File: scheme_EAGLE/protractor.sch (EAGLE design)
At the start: 2 parts

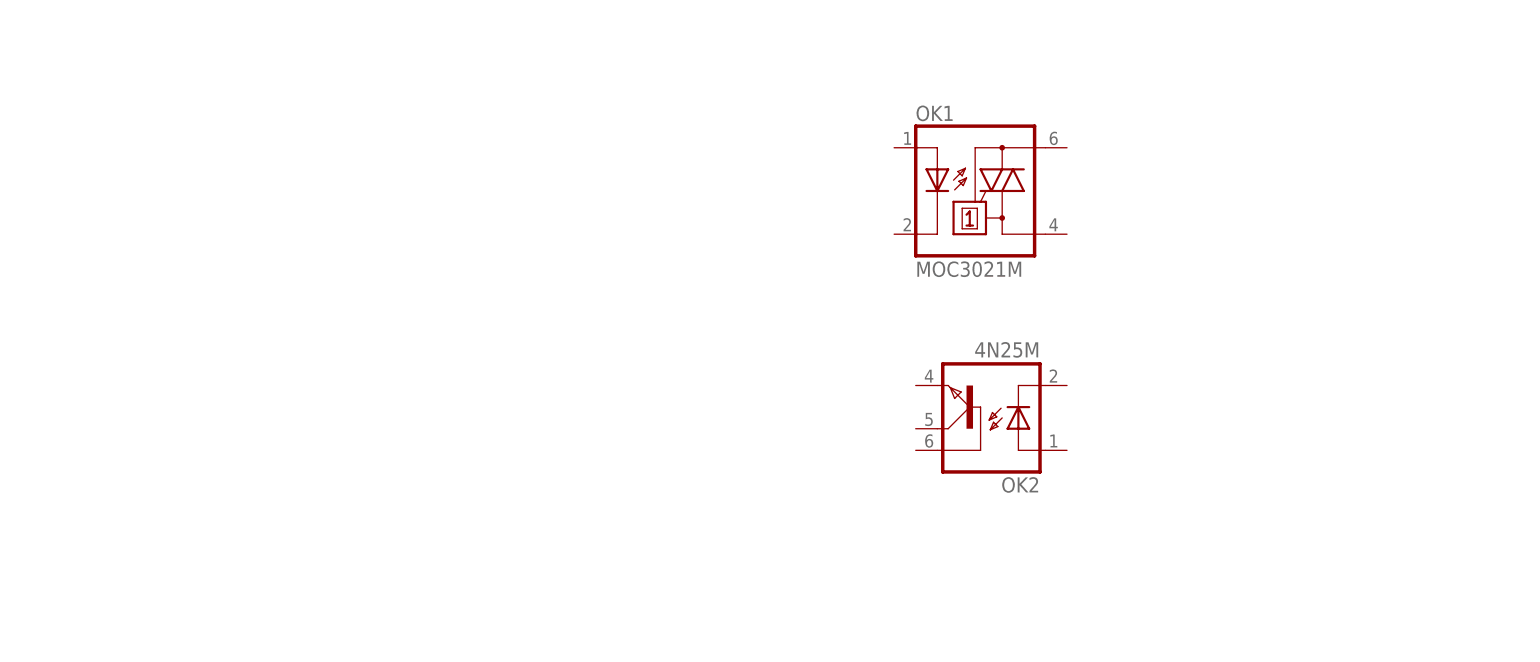
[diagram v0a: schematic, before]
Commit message: Added the bridge retifier and BT137.
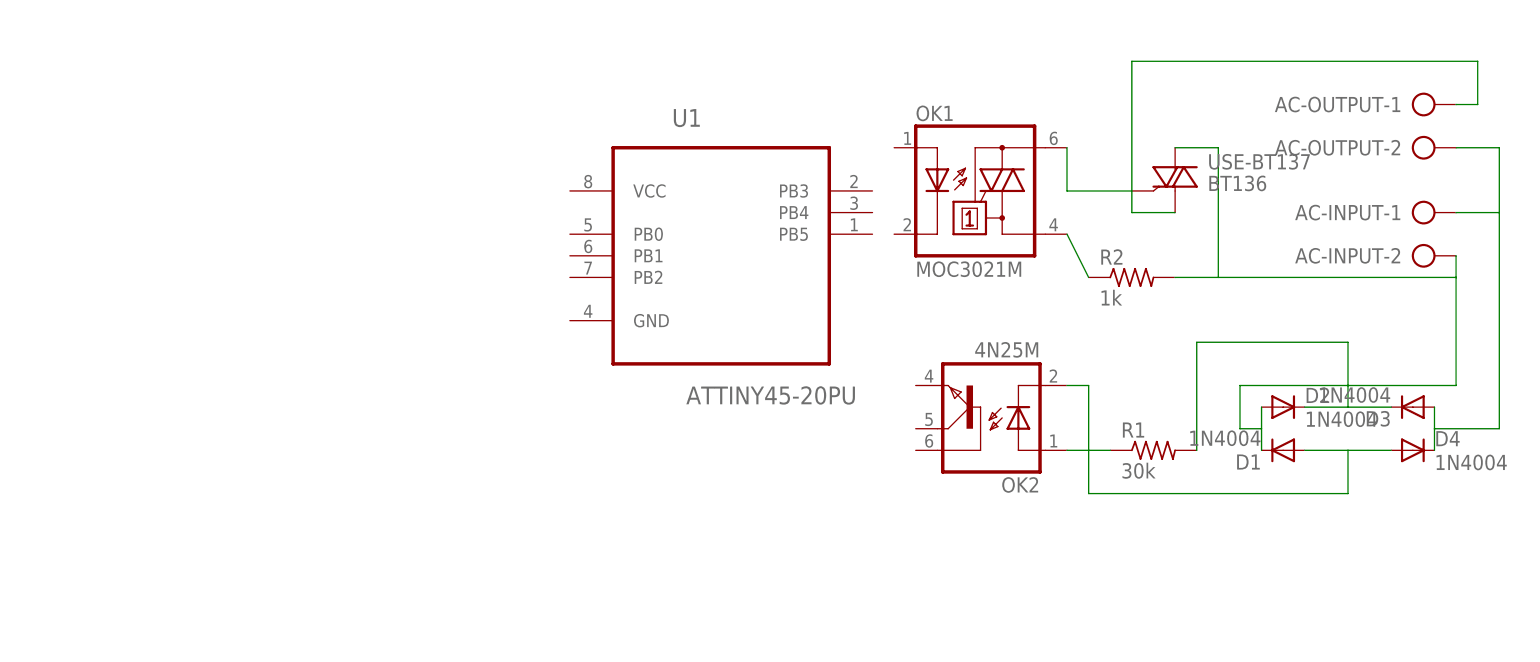
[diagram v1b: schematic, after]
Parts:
- added AC-INPUT, AC-OUTPUT: (no value), con-ptr500:AK500/2-H
- added D1, D2, D3, D4: 1N4004, adafruit:1N4004
- added R1: 30k, adafruit:R-US_0207/12
- added R2: 1k, adafruit:R-US_0207/12
- added U1: ATTINY45-20PU, Atmel_By_element14_Batch_1-00:ATTINY45-20PU
- added USE-BT137: BT136, triac:BT136
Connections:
- new net N$1: D1.A, D4.A, OK2.C
- new net N$2: D2.C, D3.C, R1.2
- new net N$3: AC-INPUT-1.KL, AC-OUTPUT-2.KL, D3.A, D4.C
- new net N$4: AC-INPUT-2.KL, D1.C, D2.A, R2.2, USE-BT137.A2
- new net N$5: OK2.A, R1.1
- new net N$6: OK1.A2, USE-BT137.G
- new net N$7: OK1.A1, R2.1
- new net N$8: AC-OUTPUT-1.KL, USE-BT137.A1

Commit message: Schema done, inserted news components.
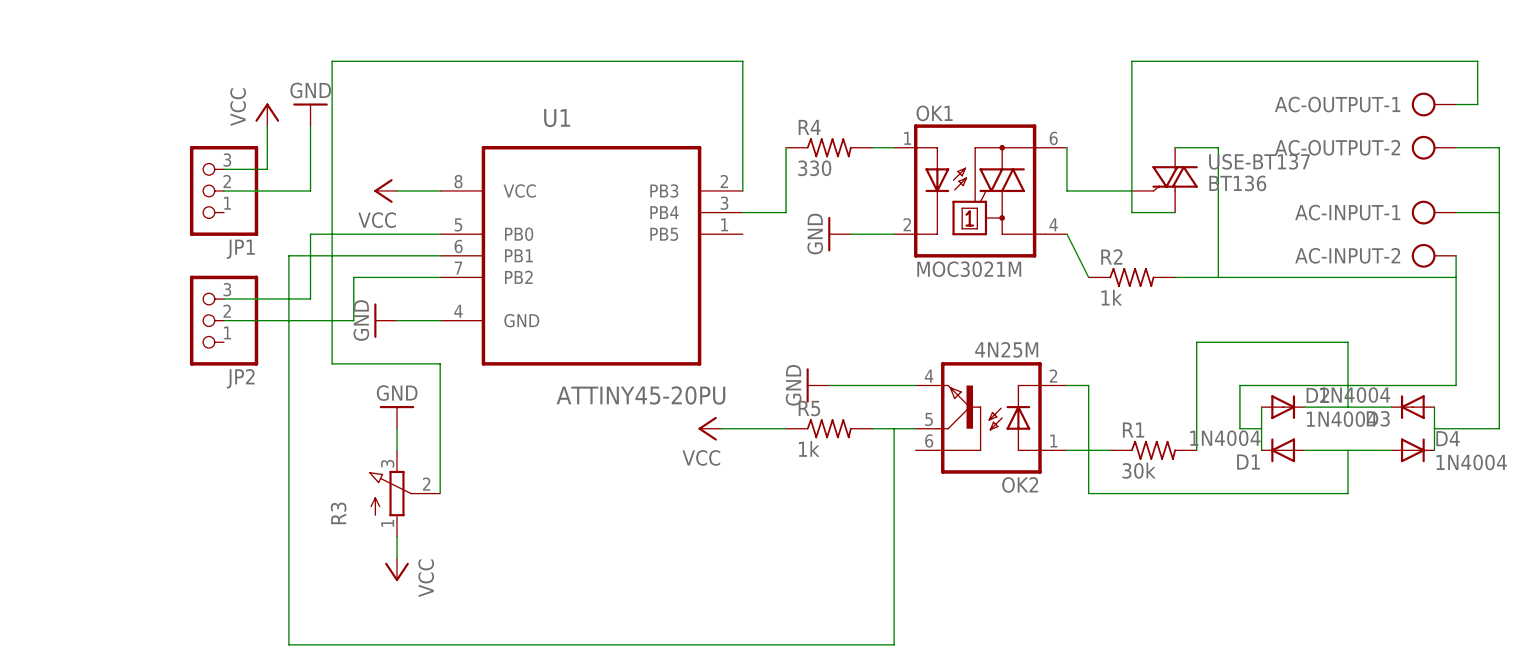
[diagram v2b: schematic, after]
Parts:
- added JP1, JP2: (no value), adafruit:PINHD-1X3
- added R3: (no value), pot:3RP/1610N
- added R4: 330, adafruit:R-US_0207/12
- added R5: 1k, adafruit:R-US_0207/12
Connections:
- new net GND: JP1.2, OK1.C, OK2.EMI, R3.E, U1.GND
- new net N$10: OK2.COL, R5.2, U1.PB1
- new net N$11: JP2.2, U1.PB2
- new net N$12: R4.1, U1.PB4
- new net N$13: OK1.A, R4.2
- new net N$14: JP2.3, U1.PB0
- new net N$9: R3.S, U1.PB3
- new net VCC: JP1.3, R3.A, R5.1, U1.VCC
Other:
- moved on the sheet: U1
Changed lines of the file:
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@@
 <part name="R2" library="adafruit" deviceset="R-US_" device="0207/12" value="1k"/>
 <part name="U1" library="Atmel_By_element14_Batch_1-00" deviceset="ATTINY45-20PU" device=""/>
+<part name="R3" library="pot" deviceset="3RP/1610N" device=""/>
+<part name="JP1" library="adafruit" deviceset="PINHD-1X3" device=""/>
+<part name="P+1" library="supply1" deviceset="VCC" device=""/>
+<part name="GND1" library="supply1" deviceset="GND" device=""/>
+<part name="GND2" library="supply1" deviceset="GND" device=""/>
+<part name="P+2" library="supply1" deviceset="VCC" device=""/>
+<part name="GND3" library="supply1" deviceset="GND" device=""/>
+<part name="P+3" library="supply1" deviceset="VCC" device=""/>
+<part name="R4" library="adafruit" deviceset="R-US_" device="0207/12" value="330"/>
+<part name="P+4" library="supply1" deviceset="VCC" device=""/>
+<part name="R5" library="adafruit" deviceset="R-US_" device="0207/12" value="1k"/>
+<part name="GND4" library="supply1" deviceset="GND" device=""/>
+<part name="GND5" library="supply1" deviceset="GND" device=""/>
+<part name="JP2" library="adafruit" deviceset="PINHD-1X3" device=""/>
 </parts>
 <sheets>
@@
 <instance part="AC-INPUT" gate="-2" x="104.14" y="68.58"/>
 <instance part="R2" gate="G$1" x="71.12" y="66.04"/>
-<instance part="U1" gate="A" x="22.86" y="71.12"/>
+<instance part="U1" gate="A" x="7.62" y="71.12"/>
+<instance part="R3" gate="G$1" x="-15.24" y="40.64"/>
+<instance part="JP1" gate="A" x="-38.1" y="76.2" rot="R180"/>
+<instance part="P+1" gate="VCC" x="-30.48" y="86.36"/>
+<instance part="GND1" gate="1" x="-25.4" y="86.36" rot="R180"/>
+<instance part="GND2" gate="1" x="-15.24" y="50.8" rot="R180"/>
+<instance part="P+2" gate="VCC" x="-15.24" y="30.48" rot="R180"/>
+<instance part="GND3" gate="1" x="-17.78" y="60.96" rot="R270"/>
+<instance part="P+3" gate="VCC" x="-17.78" y="76.2" rot="R90"/>
+<instance part="R4" gate="G$1" x="35.56" y="81.28"/>
+<instance part="P+4" gate="VCC" x="20.32" y="48.26" rot="R90"/>
+<instance part="R5" gate="G$1" x="35.56" y="48.26"/>
+<instance part="GND4" gate="1" x="33.02" y="53.34" rot="R270"/>
+<instance part="GND5" gate="1" x="35.56" y="71.12" rot="R270"/>
+<instance part="JP2" gate="A" x="-38.1" y="60.96" rot="R180"/>
 </instances>
 <busses>
@@
 </segment>
 </net>
+<net name="N$9" class="0">
+<segment>
+<pinref part="R3" gate="G$1" pin="S"/>
+<wire x1="-10.16" y1="40.64" x2="-10.16" y2="55.88" width="0.1524" layer="91"/>
+<wire x1="-10.16" y1="55.88" x2="-22.86" y2="55.88" width="0.1524" layer="91"/>
+<wire x1="-22.86" y1="55.88" x2="-22.86" y2="91.44" width="0.1524" layer="91"/>
+<pinref part="U1" gate="A" pin="PB3"/>
+<wire x1="-22.86" y1="91.44" x2="25.4" y2="91.44" width="0.1524" layer="91"/>
+<wire x1="25.4" y1="91.44" x2="25.4" y2="76.2" width="0.1524" layer="91"/>
+</segment>
+</net>
+<net name="GND" class="0">
+<segment>
+<pinref part="R3" gate="G$1" pin="E"/>
+<pinref part="GND2" gate="1" pin="GND"/>
+<wire x1="-15.24" y1="48.26" x2="-15.24" y2="45.72" width="0.1524" layer="91"/>
+</segment>
+<segment>
+<pinref part="JP1" gate="A" pin="2"/>
+<pinref part="GND1" gate="1" pin="GND"/>
+<wire x1="-35.56" y1="76.2" x2="-25.4" y2="76.2" width="0.1524" layer="91"/>
+<wire x1="-25.4" y1="76.2" x2="-25.4" y2="83.82" width="0.1524" layer="91"/>
+</segment>
+<segment>
+<pinref part="U1" gate="A" pin="GND"/>
+<pinref part="GND3" gate="1" pin="GND"/>
+<wire x1="-10.16" y1="60.96" x2="-15.24" y2="60.96" width="0.1524" layer="91"/>
+</segment>
+<segment>
+<pinref part="OK2" gate="G$1" pin="EMI"/>
+<pinref part="GND4" gate="1" pin="GND"/>
+<wire x1="45.72" y1="53.34" x2="35.56" y2="53.34" width="0.1524" layer="91"/>
+</segment>
+<segment>
+<pinref part="OK1" gate="-1" pin="C"/>
+<pinref part="GND5" gate="1" pin="GND"/>
+<wire x1="43.18" y1="71.12" x2="38.1" y2="71.12" width="0.1524" layer="91"/>
+</segment>
+</net>
+<net name="VCC" class="0">
+<segment>
+<pinref part="R3" gate="G$1" pin="A"/>
+<pinref part="P+2" gate="VCC" pin="VCC"/>
+<wire x1="-15.24" y1="35.56" x2="-15.24" y2="33.02" width="0.1524" layer="91"/>
+</segment>
+<segment>
+<pinref part="JP1" gate="A" pin="3"/>
+<pinref part="P+1" gate="VCC" pin="VCC"/>
+<wire x1="-35.56" y1="78.74" x2="-30.48" y2="78.74" width="0.1524" layer="91"/>
+<wire x1="-30.48" y1="78.74" x2="-30.48" y2="83.82" width="0.1524" layer="91"/>
+</segment>
+<segment>
+<pinref part="U1" gate="A" pin="VCC"/>
+<pinref part="P+3" gate="VCC" pin="VCC"/>
+<wire x1="-10.16" y1="76.2" x2="-15.24" y2="76.2" width="0.1524" layer="91"/>
+</segment>
+<segment>
+<pinref part="R5" gate="G$1" pin="1"/>
+<pinref part="P+4" gate="VCC" pin="VCC"/>
+<wire x1="30.48" y1="48.26" x2="22.86" y2="48.26" width="0.1524" layer="91"/>
+</segment>
+</net>
+<net name="N$10" class="0">
+<segment>
+<pinref part="R5" gate="G$1" pin="2"/>
+<pinref part="OK2" gate="G$1" pin="COL"/>
+<wire x1="40.64" y1="48.26" x2="43.18" y2="48.26" width="0.1524" layer="91"/>
+<pinref part="U1" gate="A" pin="PB1"/>
+<wire x1="43.18" y1="48.26" x2="45.72" y2="48.26" width="0.1524" layer="91"/>
+<wire x1="-10.16" y1="68.58" x2="-27.94" y2="68.58" width="0.1524" layer="91"/>
+<wire x1="-27.94" y1="68.58" x2="-27.94" y2="22.86" width="0.1524" layer="91"/>
+<wire x1="-27.94" y1="22.86" x2="43.18" y2="22.86" width="0.1524" layer="91"/>
+<wire x1="43.18" y1="22.86" x2="43.18" y2="48.26" width="0.1524" layer="91"/>
+</segment>
+</net>
+<net name="N$12" class="0">
+<segment>
+<pinref part="U1" gate="A" pin="PB4"/>
+<pinref part="R4" gate="G$1" pin="1"/>
+<wire x1="25.4" y1="73.66" x2="30.48" y2="73.66" width="0.1524" layer="91"/>
+<wire x1="30.48" y1="73.66" x2="30.48" y2="81.28" width="0.1524" layer="91"/>
+</segment>
+</net>
+<net name="N$13" class="0">
+<segment>
+<pinref part="R4" gate="G$1" pin="2"/>
+<pinref part="OK1" gate="-1" pin="A"/>
+<wire x1="40.64" y1="81.28" x2="43.18" y2="81.28" width="0.1524" layer="91"/>
+</segment>
+</net>
+<net name="N$14" class="0">
+<segment>
+<pinref part="JP2" gate="A" pin="3"/>
+<wire x1="-35.56" y1="63.5" x2="-25.4" y2="63.5" width="0.1524" layer="91"/>
+<wire x1="-25.4" y1="63.5" x2="-25.4" y2="71.12" width="0.1524" layer="91"/>
+<pinref part="U1" gate="A" pin="PB0"/>
+<wire x1="-25.4" y1="71.12" x2="-10.16" y2="71.12" width="0.1524" layer="91"/>
+</segment>
+</net>
+<net name="N$11" class="0">
+<segment>
+<pinref part="JP2" gate="A" pin="2"/>
+<wire x1="-35.56" y1="60.96" x2="-20.32" y2="60.96" width="0.1524" layer="91"/>
+<wire x1="-20.32" y1="60.96" x2="-20.32" y2="66.04" width="0.1524" layer="91"/>
+<pinref part="U1" gate="A" pin="PB2"/>
+<wire x1="-20.32" y1="66.04" x2="-10.16" y2="66.04" width="0.1524" layer="91"/>
+</segment>
+</net>

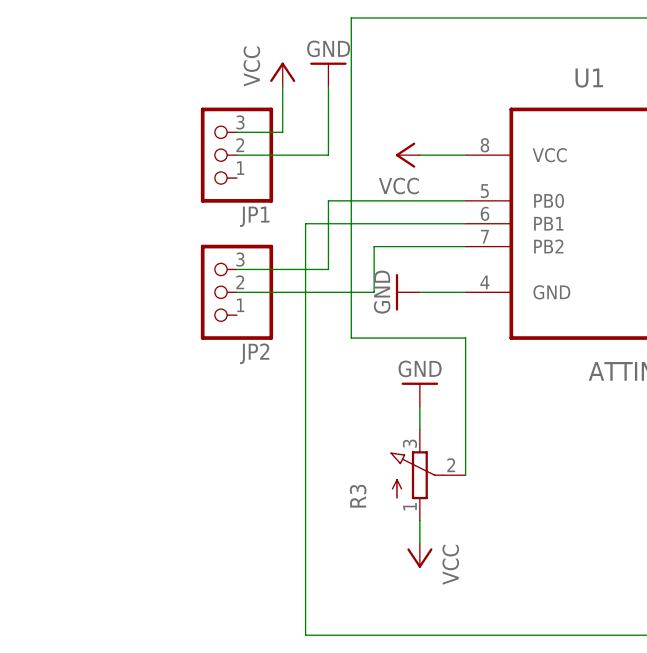
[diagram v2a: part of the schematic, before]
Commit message: Inserted the switch to choose between Arduino Comands and Potentiometer
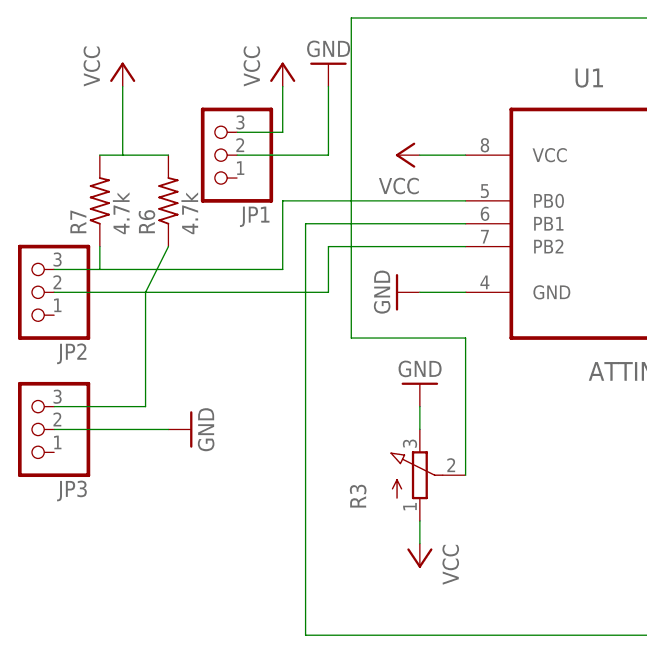
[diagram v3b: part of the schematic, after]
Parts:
- added JP3: (no value), adafruit:PINHD-1X3
- added R6, R7: 4.7k, adafruit:R-US_0207/12
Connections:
- net GND: now also JP3.2
- net N$11: now also JP2.3, R7.1, U1.PB0; no longer JP2.2, U1.PB2
- net N$14: now also JP2.2, JP3.3, R6.1, U1.PB2; no longer JP2.3, U1.PB0
- net VCC: now also R6.2, R7.2
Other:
- moved on the sheet: JP2
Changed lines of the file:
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@@
 <part name="GND5" library="supply1" deviceset="GND" device=""/>
 <part name="JP2" library="adafruit" deviceset="PINHD-1X3" device=""/>
+<part name="JP3" library="adafruit" deviceset="PINHD-1X3" device=""/>
+<part name="R6" library="adafruit" deviceset="R-US_" device="0207/12" value="4.7k"/>
+<part name="R7" library="adafruit" deviceset="R-US_" device="0207/12" value="4.7k"/>
+<part name="P+5" library="supply1" deviceset="VCC" device=""/>
+<part name="GND6" library="supply1" deviceset="GND" device=""/>
 </parts>
 <sheets>
@@
 <instance part="GND4" gate="1" x="33.02" y="53.34" rot="R270"/>
 <instance part="GND5" gate="1" x="35.56" y="71.12" rot="R270"/>
-<instance part="JP2" gate="A" x="-38.1" y="60.96" rot="R180"/>
+<instance part="JP2" gate="A" x="-58.42" y="60.96" rot="R180"/>
+<instance part="JP3" gate="A" x="-58.42" y="45.72" rot="R180"/>
+<instance part="R6" gate="G$1" x="-43.18" y="71.12" rot="R90"/>
+<instance part="R7" gate="G$1" x="-50.8" y="71.12" rot="R90"/>
+<instance part="P+5" gate="VCC" x="-48.26" y="86.36"/>
+<instance part="GND6" gate="1" x="-40.64" y="45.72" rot="R90"/>
 </instances>
 <busses>
@@
 <wire x1="43.18" y1="71.12" x2="38.1" y2="71.12" width="0.1524" layer="91"/>
 </segment>
+<segment>
+<pinref part="JP3" gate="A" pin="2"/>
+<wire x1="-55.88" y1="45.72" x2="-43.18" y2="45.72" width="0.1524" layer="91"/>
+<pinref part="GND6" gate="1" pin="GND"/>
+</segment>
 </net>
 <net name="VCC" class="0">
@@
 <pinref part="P+4" gate="VCC" pin="VCC"/>
 <wire x1="30.48" y1="48.26" x2="22.86" y2="48.26" width="0.1524" layer="91"/>
+</segment>
+<segment>
+<pinref part="R7" gate="G$1" pin="2"/>
+<pinref part="R6" gate="G$1" pin="2"/>
+<wire x1="-50.8" y1="76.2" x2="-48.26" y2="76.2" width="0.1524" layer="91"/>
+<pinref part="P+5" gate="VCC" pin="VCC"/>
+<wire x1="-48.26" y1="76.2" x2="-43.18" y2="76.2" width="0.1524" layer="91"/>
+<wire x1="-48.26" y1="83.82" x2="-48.26" y2="76.2" width="0.1524" layer="91"/>
 </segment>
 </net>
@@
 </segment>
 </net>
+<net name="N$11" class="0">
+<segment>
+<pinref part="JP2" gate="A" pin="3"/>
+<pinref part="R7" gate="G$1" pin="1"/>
+<wire x1="-55.88" y1="63.5" x2="-50.8" y2="63.5" width="0.1524" layer="91"/>
+<wire x1="-50.8" y1="63.5" x2="-50.8" y2="66.04" width="0.1524" layer="91"/>
+<wire x1="-50.8" y1="63.5" x2="-30.48" y2="63.5" width="0.1524" layer="91"/>
+<wire x1="-30.48" y1="63.5" x2="-30.48" y2="71.12" width="0.1524" layer="91"/>
+<pinref part="U1" gate="A" pin="PB0"/>
+<wire x1="-30.48" y1="71.12" x2="-10.16" y2="71.12" width="0.1524" layer="91"/>
+</segment>
+</net>
 <net name="N$14" class="0">
 <segment>
-<pinref part="JP2" gate="A" pin="3"/>
-<wire x1="-35.56" y1="63.5" x2="-25.4" y2="63.5" width="0.1524" layer="91"/>
-<wire x1="-25.4" y1="63.5" x2="-25.4" y2="71.12" width="0.1524" layer="91"/>
-<pinref part="U1" gate="A" pin="PB0"/>
-<wire x1="-25.4" y1="71.12" x2="-10.16" y2="71.12" width="0.1524" layer="91"/>
-</segment>
-</net>
-<net name="N$11" class="0">
-<segment>
 <pinref part="JP2" gate="A" pin="2"/>
-<wire x1="-35.56" y1="60.96" x2="-20.32" y2="60.96" width="0.1524" layer="91"/>
-<wire x1="-20.32" y1="60.96" x2="-20.32" y2="66.04" width="0.1524" layer="91"/>
+<pinref part="R6" gate="G$1" pin="1"/>
+<wire x1="-55.88" y1="60.96" x2="-45.72" y2="60.96" width="0.1524" layer="91"/>
+<wire x1="-45.72" y1="60.96" x2="-43.18" y2="66.04" width="0.1524" layer="91"/>
+<wire x1="-45.72" y1="60.96" x2="-25.4" y2="60.96" width="0.1524" layer="91"/>
+<wire x1="-25.4" y1="60.96" x2="-25.4" y2="66.04" width="0.1524" layer="91"/>
 <pinref part="U1" gate="A" pin="PB2"/>
-<wire x1="-20.32" y1="66.04" x2="-10.16" y2="66.04" width="0.1524" layer="91"/>
-</segment>
-</net>
+<wire x1="-25.4" y1="66.04" x2="-10.16" y2="66.04" width="0.1524" layer="91"/>
+<pinref part="JP3" gate="A" pin="3"/>
+<wire x1="-55.88" y1="48.26" x2="-45.72" y2="48.26" width="0.1524" layer="91"/>
+<wire x1="-45.72" y1="48.26" x2="-45.72" y2="60.96" width="0.1524" layer="91"/>
+</segment>
+</net>

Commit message: I added coments, and pullup for i2c comunication.
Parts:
- renumbered USE-BT137 to BT1
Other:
- note added: "For 800w, use the BT137."
- note added: "I choosed the ATtiny45 for the scheme, but i use 85."
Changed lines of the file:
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@@
 <part name="D4" library="adafruit" deviceset="1N4004" device=""/>
 <part name="R1" library="adafruit" deviceset="R-US_" device="0207/12" value="30k"/>
-<part name="USE-BT137" library="triac" deviceset="BT136" device=""/>
+<part name="BT1" library="triac" deviceset="BT136" device=""/>
 <part name="AC-OUTPUT" library="con-ptr500" deviceset="AK500/2-H" device=""/>
 <part name="AC-INPUT" library="con-ptr500" deviceset="AK500/2-H" device=""/>
@@
 <sheet>
 <plain>
+<text x="66.04" y="93.98" size="1.778" layer="91">For 800w, use the BT137.</text>
+<text x="-15.24" y="93.98" size="1.778" layer="91">I choosed the ATtiny45 for the scheme, but i use 85. </text>
 </plain>
 <instances>
@@
 <instance part="D4" gate="1" x="104.14" y="45.72"/>
 <instance part="R1" gate="G$1" x="73.66" y="45.72"/>
-<instance part="USE-BT137" gate="-1" x="76.2" y="76.2"/>
+<instance part="BT1" gate="-1" x="76.2" y="76.2"/>
 <instance part="AC-OUTPUT" gate="-1" x="104.14" y="86.36"/>
 <instance part="AC-OUTPUT" gate="-2" x="104.14" y="81.28"/>
@@
 <wire x1="109.22" y1="66.04" x2="109.22" y2="68.58" width="0.1524" layer="91"/>
 <wire x1="76.2" y1="66.04" x2="81.28" y2="66.04" width="0.1524" layer="91"/>
-<pinref part="USE-BT137" gate="-1" pin="A2"/>
+<pinref part="BT1" gate="-1" pin="A2"/>
 <wire x1="81.28" y1="66.04" x2="109.22" y2="66.04" width="0.1524" layer="91"/>
 <wire x1="76.2" y1="81.28" x2="81.28" y2="81.28" width="0.1524" layer="91"/>
@@
 <net name="N$6" class="0">
 <segment>
-<pinref part="USE-BT137" gate="-1" pin="G"/>
+<pinref part="BT1" gate="-1" pin="G"/>
 <pinref part="OK1" gate="-1" pin="A2"/>
 <wire x1="71.12" y1="76.2" x2="63.5" y2="76.2" width="0.1524" layer="91"/>
@@
 <net name="N$8" class="0">
 <segment>
-<pinref part="USE-BT137" gate="-1" pin="A1"/>
+<pinref part="BT1" gate="-1" pin="A1"/>
 <wire x1="76.2" y1="73.66" x2="71.12" y2="73.66" width="0.1524" layer="91"/>
 <wire x1="71.12" y1="73.66" x2="71.12" y2="91.44" width="0.1524" layer="91"/>
